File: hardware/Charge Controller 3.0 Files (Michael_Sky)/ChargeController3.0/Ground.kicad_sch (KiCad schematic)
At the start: 6 parts

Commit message: Added template, reassigned pins
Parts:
- R1: footprint (none) -> Resistor_SMD:R_0201_0603Metric
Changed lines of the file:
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@@
 			)
 		)
-		(property "Footprint" ""
+		(property "Footprint" "Resistor_SMD:R_0201_0603Metric"
 			(at 108.712 101.6 90)
 			(hide yes)

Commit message: New formatting
New formatting
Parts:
- C1: footprint (none) -> Capacitor_SMD:C_0402_1005Metric
- H1, H2, H3: footprint (none) -> MountingHole:MountingHole_3.2mm_M3_ISO14580
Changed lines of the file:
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@@
 			)
 		)
-		(property "Footprint" ""
+		(property "Footprint" "MountingHole:MountingHole_3.2mm_M3_ISO14580"
 			(at 184.15 88.9 0)
 			(hide yes)
@@
 			)
 		)
-		(property "Footprint" ""
+		(property "Footprint" "Capacitor_SMD:C_0402_1005Metric"
 			(at 120.3452 105.41 0)
 			(hide yes)
@@
 			)
 		)
-		(property "Footprint" ""
+		(property "Footprint" "MountingHole:MountingHole_3.2mm_M3_ISO14580"
 			(at 163.83 88.9 0)
 			(hide yes)
@@
 			)
 		)
-		(property "Footprint" ""
+		(property "Footprint" "MountingHole:MountingHole_3.2mm_M3_ISO14580"
 			(at 142.24 88.9 0)
 			(hide yes)

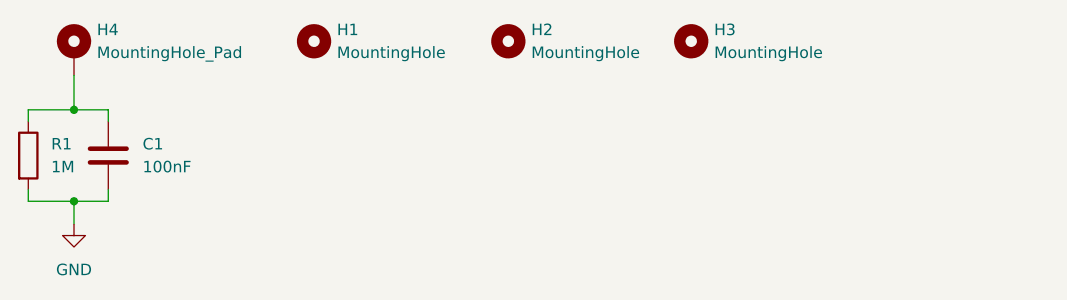
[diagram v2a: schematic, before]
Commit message: Final PCB?
inhibits rework, filtering rework
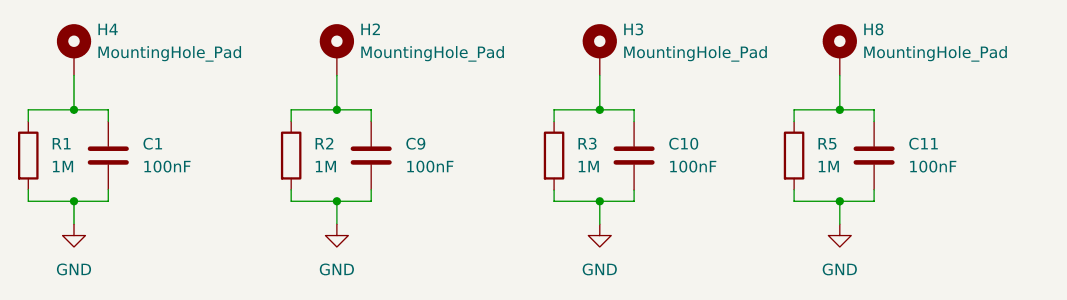
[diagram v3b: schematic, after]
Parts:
- removed H1, H2, H3: MountingHole, MountingHole:MountingHole_3.2mm_M3_ISO14580, symbol Mechanical:MountingHole
- added C10, C11, C9: 100nF, Capacitor_SMD:C_0402_1005Metric, symbol Device:C
- added H2, H3, H8: MountingHole_Pad, MountingHole:MountingHole_3.2mm_M3_ISO14580_Pad, symbol Mechanical:MountingHole_Pad
- added R2, R3, R5: 1M, Resistor_SMD:R_0201_0603Metric, symbol Device:R
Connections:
- net GND: now also C10.2, C11.2, C9.2, R2.2, R3.2, R5.2
- new net: C9.1, H2.1, R2.1
- new net: C11.1, H8.1, R5.1
- new net: C10.1, H3.1, R3.1
